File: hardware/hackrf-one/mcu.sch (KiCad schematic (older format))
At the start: 113 parts, among them J1 GSG-USB-MICRO-B, P1 1V8, P10 CTOUT_2, P11 CTIN_2, P20 GPIO, P21 ANALOG, P22 I2S, P23 DBGEN, P24 TRST, P25 LPC_ISP, P26 LPC_JTAG, P28 SD, P29 CPLD_JTAG, P3 GND, P30 BANK2_AUX, P31 BANK1_AUX, P35 GCK0, P5 WAKEUP, P6 TRACECLK, P7 CTIN_4, P8 VCC, P9 CTOUT_4, SW1 DFU, SW2 RESET, U20 W25Q80BV, U21 TPS62410, U22 GSG-IP4220CZ6, U23 LPC43XXFBD144, U24 GSG-XC2C64A-7VQG100C, X2 MCU_XTAL

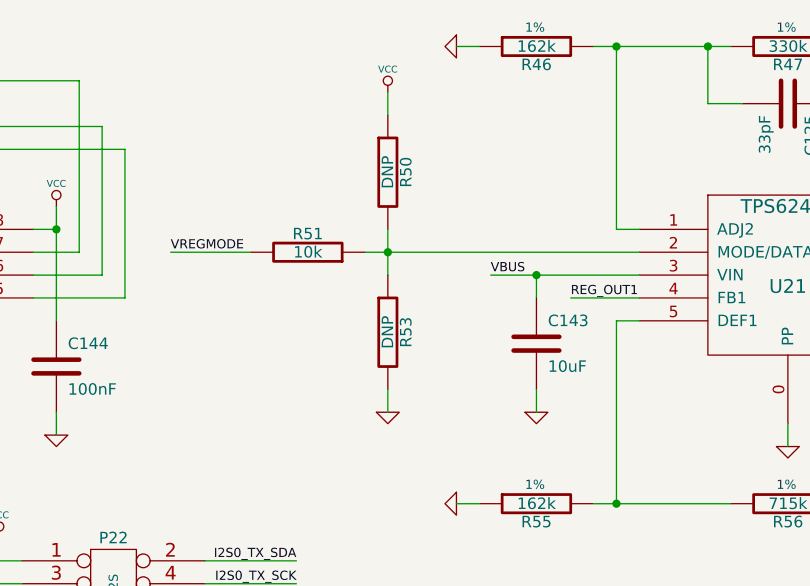
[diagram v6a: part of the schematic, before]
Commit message: removed more DNP parts
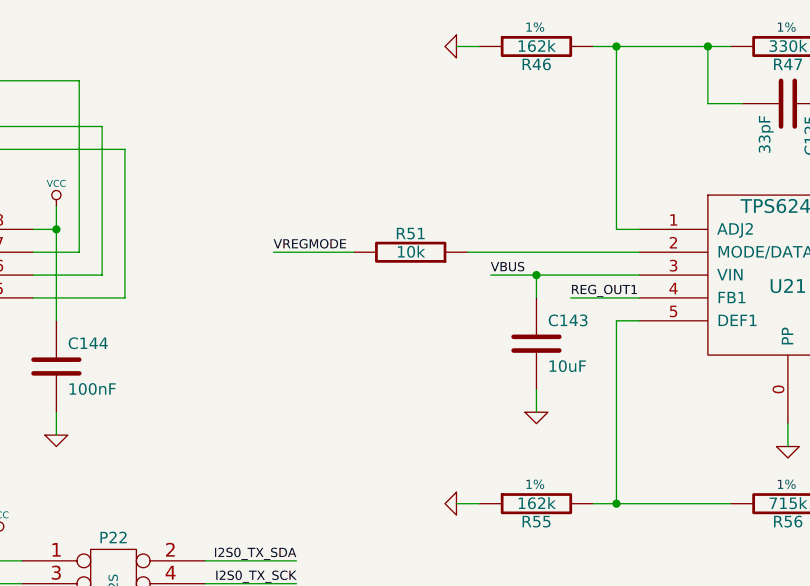
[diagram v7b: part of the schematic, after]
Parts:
- removed R50, R53: DNP, symbol R
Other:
- moved on the sheet: R51

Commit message: optional RTC XTAL
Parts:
- added C? (x2): 12pF, symbol C
- added X?: CRYSTAL, symbol CRYSTAL
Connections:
- net GND: now also C?.2, C?.2
- net VCC: no longer U23.127 (VBAT)
- net RTCX1: now reaches U23.125 (RTCX1)
- net RTCX1: now also C?.1, X?.1
- net RTCX2: now reaches U23.126 (RTCX2)
- net RTCX2: now also C?.1, X?.2
- no-connect marks 31 -> 28
